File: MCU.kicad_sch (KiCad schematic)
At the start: 62 parts, among them J1 GPS, J2 GPS, Q1 SI2312BDS, Q2 SI2301BDS, SW1 TS2306A, U4 RP2354A, U5 W25Q128JVPIQ, U6 TPD2E001DRLR, Y1 40MHz

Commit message: Power and MCU
Updated the power schematic.
Updated the MCU schematic.

TODO:
Merge with features branch.
Review all schematics prior to layout.
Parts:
- removed BZ1: Buzzer, Custom_Parts:FUET_9018, symbol Device:Buzzer
- removed C30: 10u, Capacitor_SMD:C_0805_2012Metric, symbol Device:C
- removed D1: WS2812B, Custom_Parts:WS2812B-2020, symbol LED:WS2812B-2020
- removed D2: LED, LED_SMD:LED_0805_2012Metric, symbol Device:LED
- removed Q1: SI2312BDS, Package_TO_SOT_SMD:SOT-23, symbol Custom_Parts:SI2312BDS
- removed R16: 5.1K, Resistor_SMD:R_0603_1608Metric, symbol Device:R
- removed R20: 1K, Resistor_SMD:R_0603_1608Metric, symbol Device:R
- removed U4: RP2354A, Custom_Parts:RP2350A_QFN-60_EP_7.75x7.75_Pitch0.4mm, symbol MCU_RaspberryPi:RP2354A
- added U4: RP2354B, Custom_Parts:RP2350B_QFN-80_EP_10.573x10.573_Pitch0.4mm, symbol MCU_RaspberryPi:RP2354B
- C11: value 15p -> 10u; footprint Capacitor_SMD:C_0603_1608Metric -> Capacitor_SMD:C_0805_2012Metric
- C12: value 10u -> 15p; footprint Capacitor_SMD:C_0805_2012Metric -> Capacitor_SMD:C_0603_1608Metric
- C13: footprint Capacitor_SMD:C_0201_0603Metric -> Capacitor_SMD:C_0603_1608Metric
- C15: value 15p -> 100n
- C16: value 100n -> 15p
- C20: value 10u -> 100n; footprint Capacitor_SMD:C_0805_2012Metric -> Capacitor_SMD:C_0201_0603Metric
- C21, C25, C28: value 100n -> 10u; footprint Capacitor_SMD:C_0603_1608Metric -> Capacitor_SMD:C_0805_2012Metric
- C24, C27: value 10u -> 100n; footprint Capacitor_SMD:C_0805_2012Metric -> Capacitor_SMD:C_0603_1608Metric
- R10: value 1K -> 27
- R11: value 100 -> 27
- R12: value 100K -> 1K
- R13: value 100K -> 5.1K
- R14: value 10K -> 5.1K
- R15: value 5.1K -> R; footprint Resistor_SMD:R_0603_1608Metric -> (none)
- R7: value 27 -> 100K
- R8: value 27 -> 10K
- TP10: value GPIO19 -> RUN
- TP3: value GPS_SDA -> GPS_TX
- TP4: value GPS_SCL -> GPS_RX
- TP5: value GPS_TX -> GPS_SDA
- TP6: value GPS_RX -> GPS_SCL
- TP7: value GPIO6 -> CAM_TX
- TP8: value GPIO7 -> CAM_RX
- TP9: value GPIO18 -> CAM_SBUS
- renumbered D3 to D1, Q2 to Q1, R17 to R16, R18 to R17, R19 to R18, R21 to R19
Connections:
- net GPIO18 is gone; now on net CAM_SBUS: TP9.1
- net GPIO6 is gone; now on net CAM_TX: TP7.1
- net GPIO7 is gone; now on net CAM_RX: TP8.1
- net 1V1: now also C11.1, C28.1, U4.10 (DVDD), U4.32 (DVDD), U4.51 (DVDD), U4.65 (VREG_FB); no longer C12.1, C25.1
- net 3V3: now also C15.1, C20.1, C25.1, R11.1, R13.1, R14.1, U4.15 (IOVDD), U4.24 (IOVDD), U4.29 (IOVDD), U4.41 (IOVDD), U4.5 (IOVDD), U4.50 (IOVDD), U4.59 (ADC_AVDD), U4.60 (IOVDD), U4.64 (VREG_VIN), U4.68 (USB_OTP_VDD), U4.69 (QSPI_IOVDD), U4.76 (IOVDD); no longer C13.1, C16.1, C21.1, R8.1
- net BUZZER: now also U4.56 (GPIO45/ADC5); no longer R11.1
- net CAM_RX: now also U4.26 (GPIO25)
- net CAM_SBUS: now also U4.27 (GPIO26)
- net CAM_TX: now also U4.25 (GPIO24)
- net ESC1: now also U4.11 (GPIO12)
- net ESC2: now also U4.12 (GPIO13)
- net ESC3: now also U4.13 (GPIO14)
- net ESC4: now also U4.14 (GPIO15)
- net FLASH_SS: now also U4.77 (GPIO0)
- net GND: now also R8.2, U4.62 (VREG_PGND), U4.81 (GND); no longer R12.2, R14.2
- net GPS_RX: now also TP4.1, U4.2 (GPIO5); no longer TP6.1
- net GPS_SCL: now also TP6.1, U4.4 (GPIO7); no longer TP4.1
- net GPS_SDA: now also TP5.1, U4.3 (GPIO6); no longer TP3.1
- net GPS_TX: now also TP3.1, U4.1 (GPIO4); no longer TP5.1
- net IMU_CLK: now also U4.21 (GPIO21)
- net IMU_CS: now also U4.17 (GPIO17)
- net IMU_INT: now also U4.22 (GPIO22)
- net IMU_MISO: now also U4.16 (GPIO16)
- net IMU_MOSI: now also U4.19 (GPIO19)
- net IMU_SCLK: now also U4.18 (GPIO18)
- net LED1: now also U4.53 (GPIO42/ADC2)
- net LED2: now also U4.54 (GPIO43/ADC3)
- net QSPI_SCLK: now also U4.71 (QSPI_SCLK)
- net QSPI_SD0: now also U4.72 (QSPI_SD0)
- net QSPI_SD1: now also U4.74 (QSPI_SD1)
- net QSPI_SD2: now also U4.73 (QSPI_SD2)
- net QSPI_SD3: now also U4.70 (QSPI_SD3)
- net QSPI_SS: now also U4.75 (~{QSPI_SS})
- net SENS_SCL: now also R14.2, U4.9 (GPIO11)
- net SENS_SDA: now also R13.2, U4.8 (GPIO10); no longer R15.2
- net SWCLK: now also U4.33 (SWCLK)
- net SWDIO: now also U4.34 (SWDIO)
- net USB_D+: now also R9.2; no longer R7.2
- net USB_D-: now also R10.2; no longer R9.2
- net VBAT: now also R7.2; no longer R13.1
- net VREG_LX: now also U4.63 (VREG_LX)
- net XIN: now reaches Y1.1
- net XIN: now also C12.1, U4.30 (XIN); no longer C11.1
- net VBAT_ADC: now reaches R7.1
- net VBAT_ADC: now also C13.1, R8.1, U4.49 (GPIO40/ADC0)
- net at R9.1: now also U4.67 (USB_DP)
- net BOOT_SW: now reaches R5.1, SW1.2
- net at R12.1: now also C16.1, Y1.3; no longer R11.2
- net CC1: now reaches HH-16P-CB-TYPE-C1.A5 (CC1), R18.1
- net CC2: now reaches HH-16P-CB-TYPE-C1.B5 (CC2), R17.1
- net GPIO19 renamed RUN
- net RUN: now also R15.2, U4.35 (RUN)
- new net: R10.1, U4.66 (USB_DM)
- new net RX_BUSY: U4.42 (GPIO33)
- new net RX_CS: U4.37 (GPIO29)
- new net RX_DIO1: U4.43 (GPIO34)
- new net RX_DIO2: U4.44 (GPIO35)
- new net RX_EN: U4.45 (GPIO36)
- new net RX_MISO: U4.36 (GPIO28)
- new net RX_MOSI: U4.39 (GPIO31)
- new net RX_RST: U4.40 (GPIO32)
- new net RX_SCLK: U4.38 (GPIO30)
- new net TX_EN: U4.46 (GPIO37)
- new net VREG_AVDD: C21.1, R11.2, U4.61 (VREG_AVDD)
- new net XOUT: R12.2, U4.31 (XOUT)
- no-connect marks 4 -> 17
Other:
- company: Chapuzas S.L. -> DavidMolTor
- moved on the sheet: J1, J2

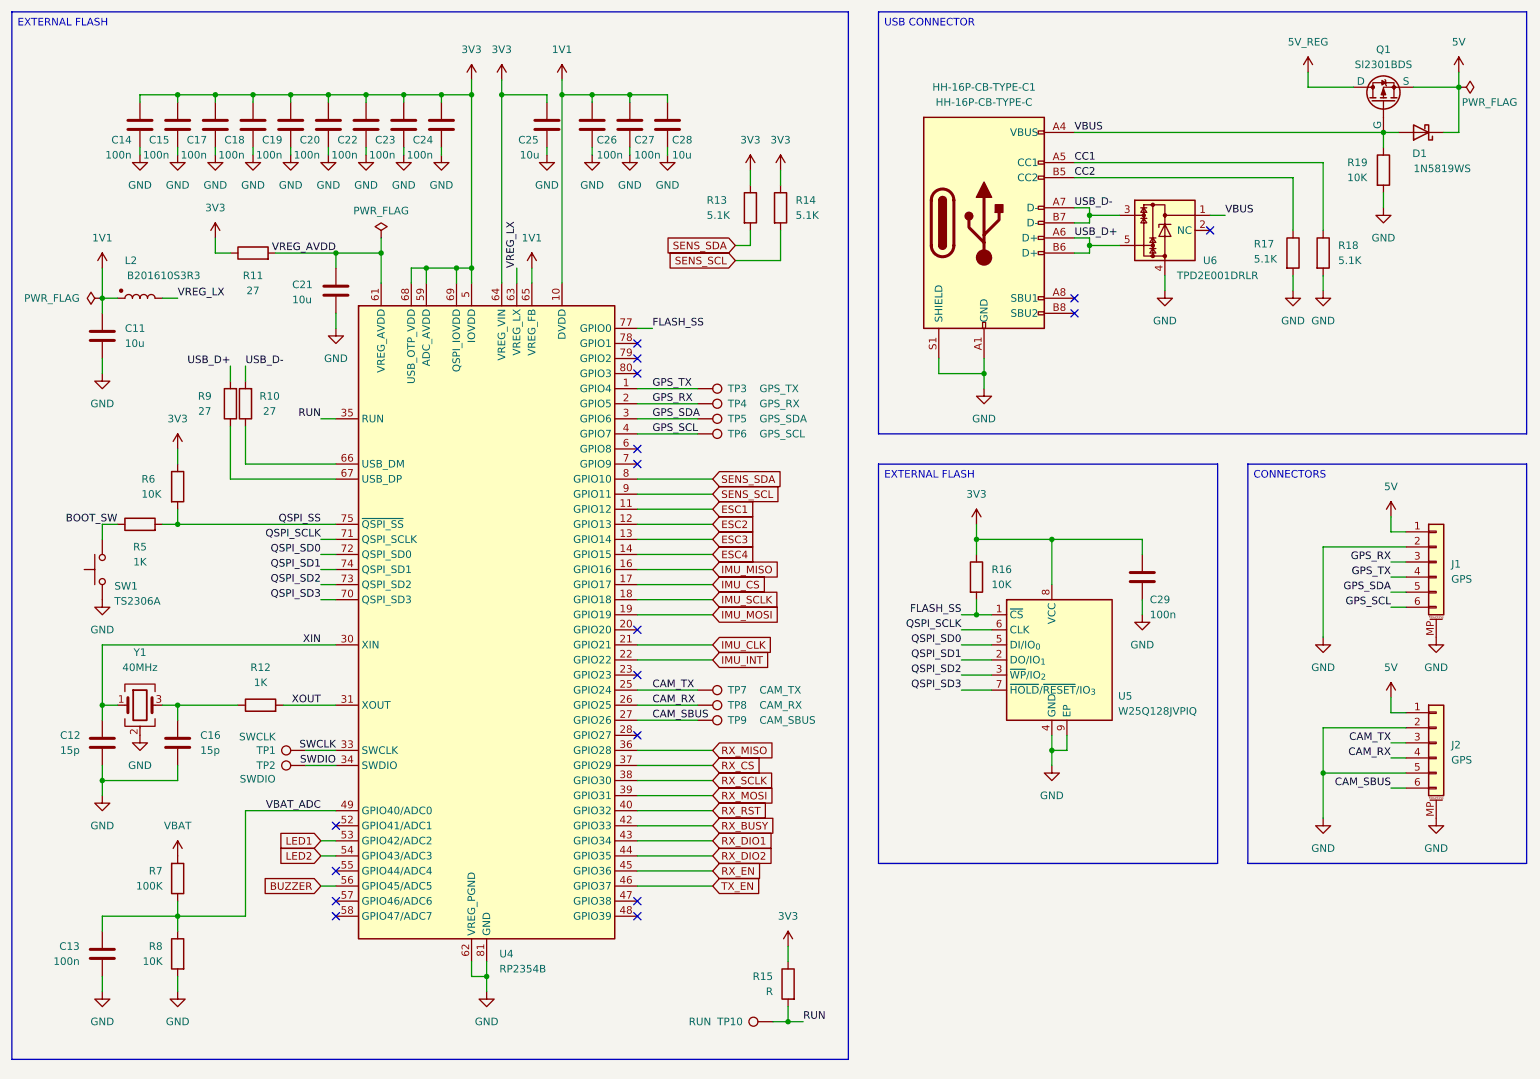
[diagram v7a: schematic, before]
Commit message: MCU design
Updated the MCU schematic.

TODO:
Add a bind button connected to the MCU.
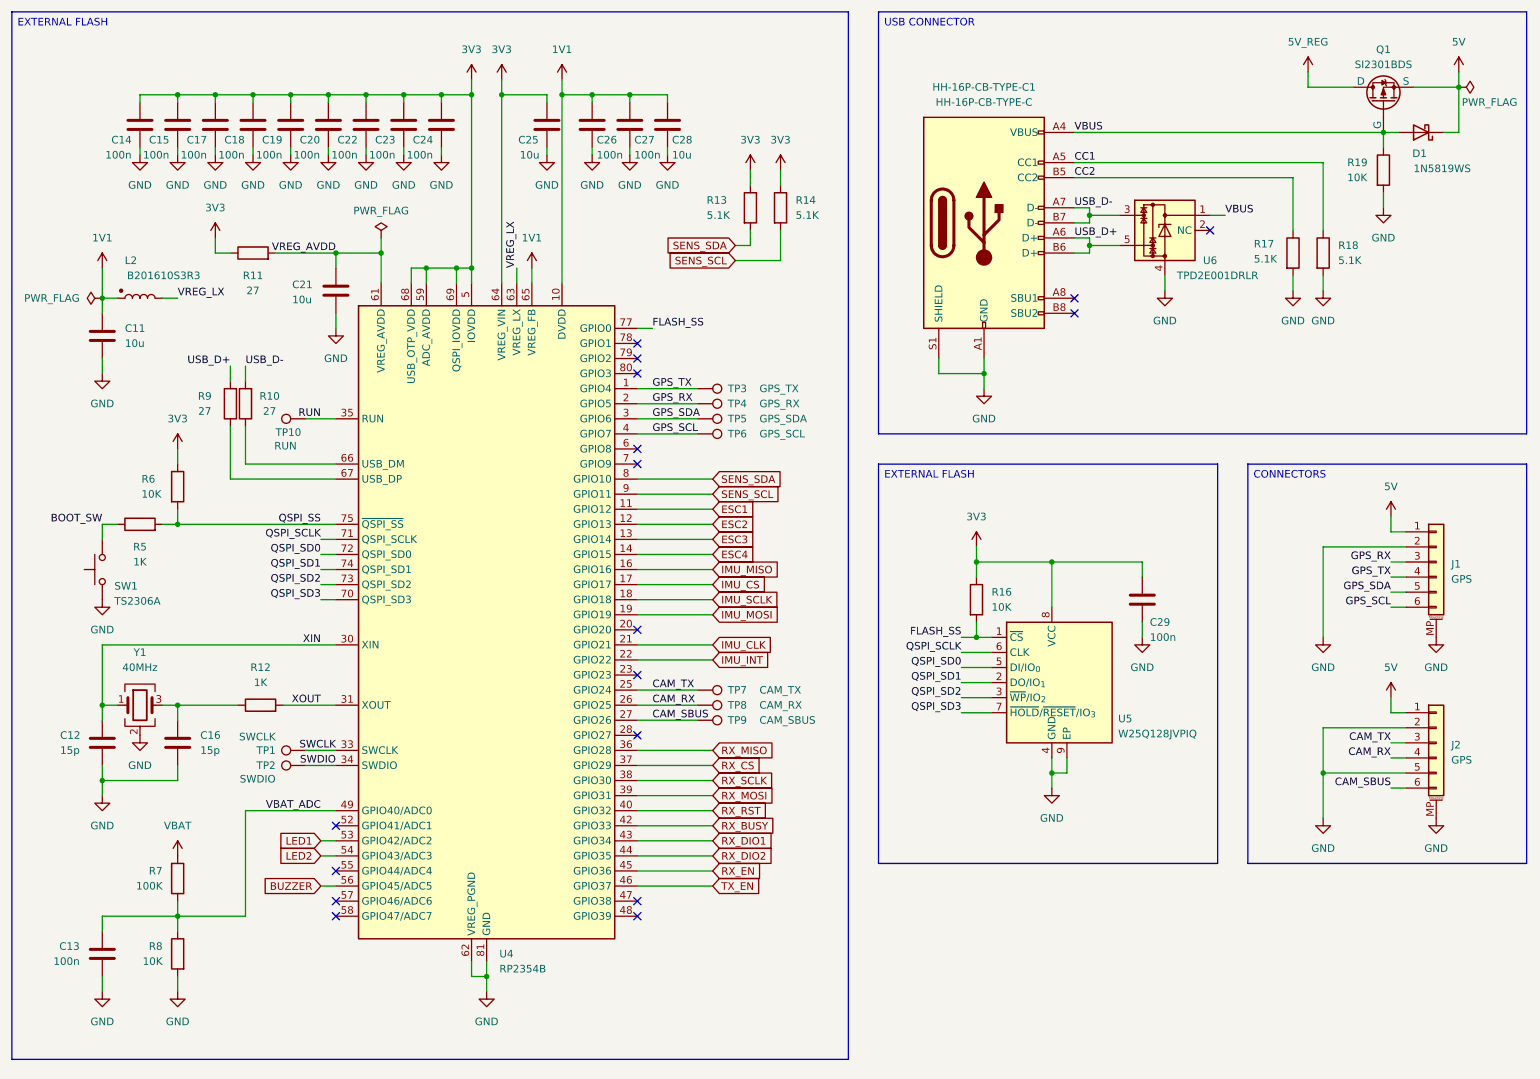
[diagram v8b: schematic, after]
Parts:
- removed R15: R, symbol Device:R
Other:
- moved on the sheet: C29, R16, TP10, U5
